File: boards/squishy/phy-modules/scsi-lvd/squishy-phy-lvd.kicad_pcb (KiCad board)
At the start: 6 copper layers, 75 x 92.5 mm, 211 parts, among them J1 SCSI PHY Mezz, J2 SCSI Connector, J3 Conn_01x04, Q1 PMDPB58UPE,115, Q2 PMDPB58UPE,115, Q3 PMDPB58UPE,115, Q4 PMDPB58UPE,115, Q5 PMDPB58UPE,115, Q6 DMN65D8L-7, U1 M24C02-RMC, U10 SN65LVDS180-Q1, U11 SN65LVDS180-Q1, U12 FIN1027A, U13 SN65LVDS180-Q1, U14 SN65LVDS180-Q1, U15 FIN1027A, U16 SN65LVDS180-Q1, U17 SN65LVDS180-Q1, U18 FIN1027A, U19 SN65LVDS180-Q1, U2 SN65LVDS180-Q1, U20 SN65LVDS180-Q1, U21 LM321, U22 SN65LVDS180-Q1, U23 SN65LVDS180-Q1, U24 FIN1027A, U25 SN65LVDS180-Q1, U26 SN65LVDS180-Q1, U27 SN65LVDS180-Q1, U28 SN65LVDS180-Q1, U29 SN65LVDS180-Q1, U3 FIN1027A, U30 SN65LVDS180-Q1, U31 SN65LVDS180-Q1, U34 FIN1027A, U35 FIN1027A, U36 FIN1027A, U37 FIN1027A, U38 UCC5640PW24, U39 LM2903, U4 SN65LVDS180-Q1, U42 SN65LVDS180-Q1, U43 SN65LVDS180-Q1, U44 SN65LVDS180-Q1, U45 SN65LVDS180-Q1, U47 SN65LVDS180-Q1, U5 SN65LVDS180-Q1, U50 UCC5640PW24, U51 UCC5640PW24, U6 FIN1027A, U7 SN65LVDS180-Q1, U8 SN65LVDS180-Q1, U9 FIN1027A

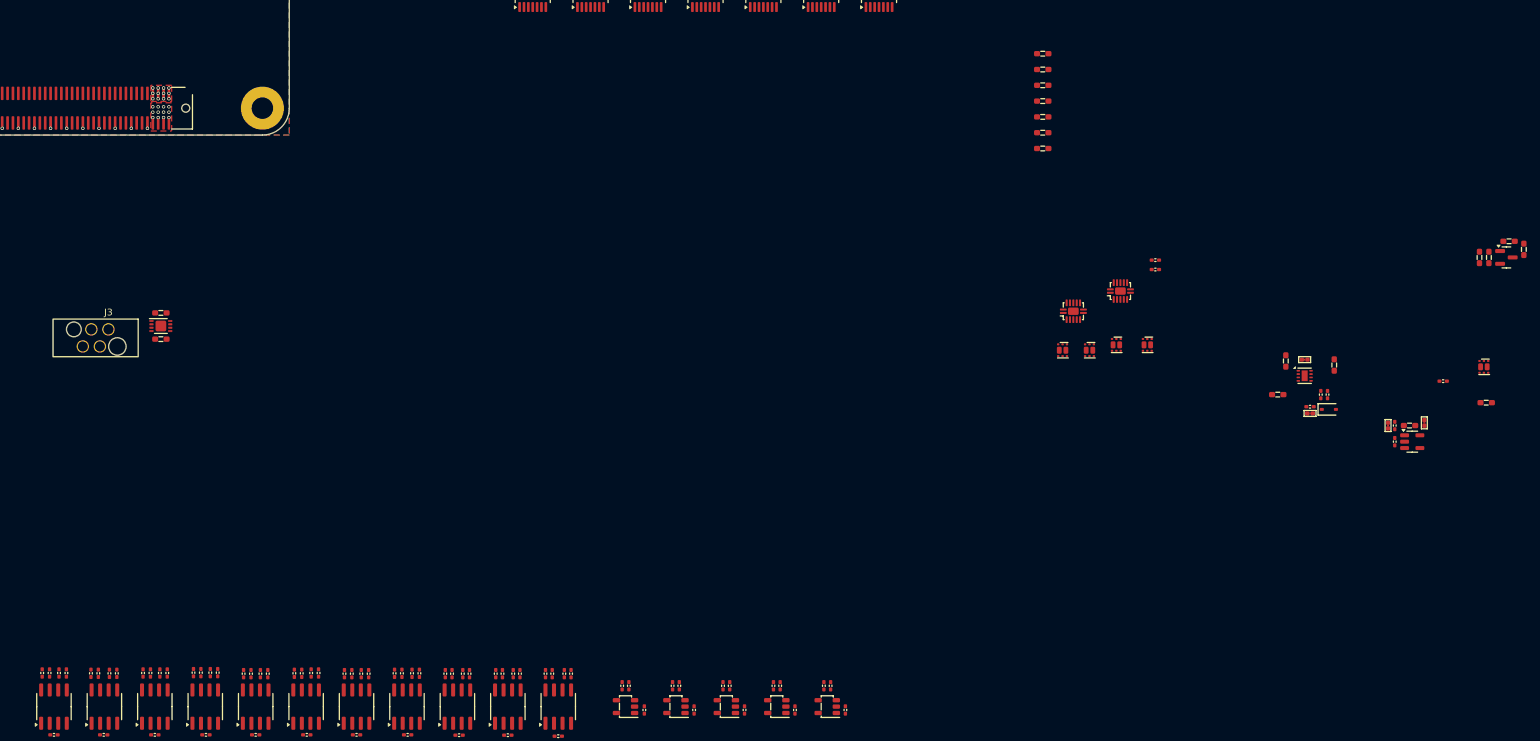
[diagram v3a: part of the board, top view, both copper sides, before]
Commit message: squishy:  phy: lvd: Upgraded to KiCad v9
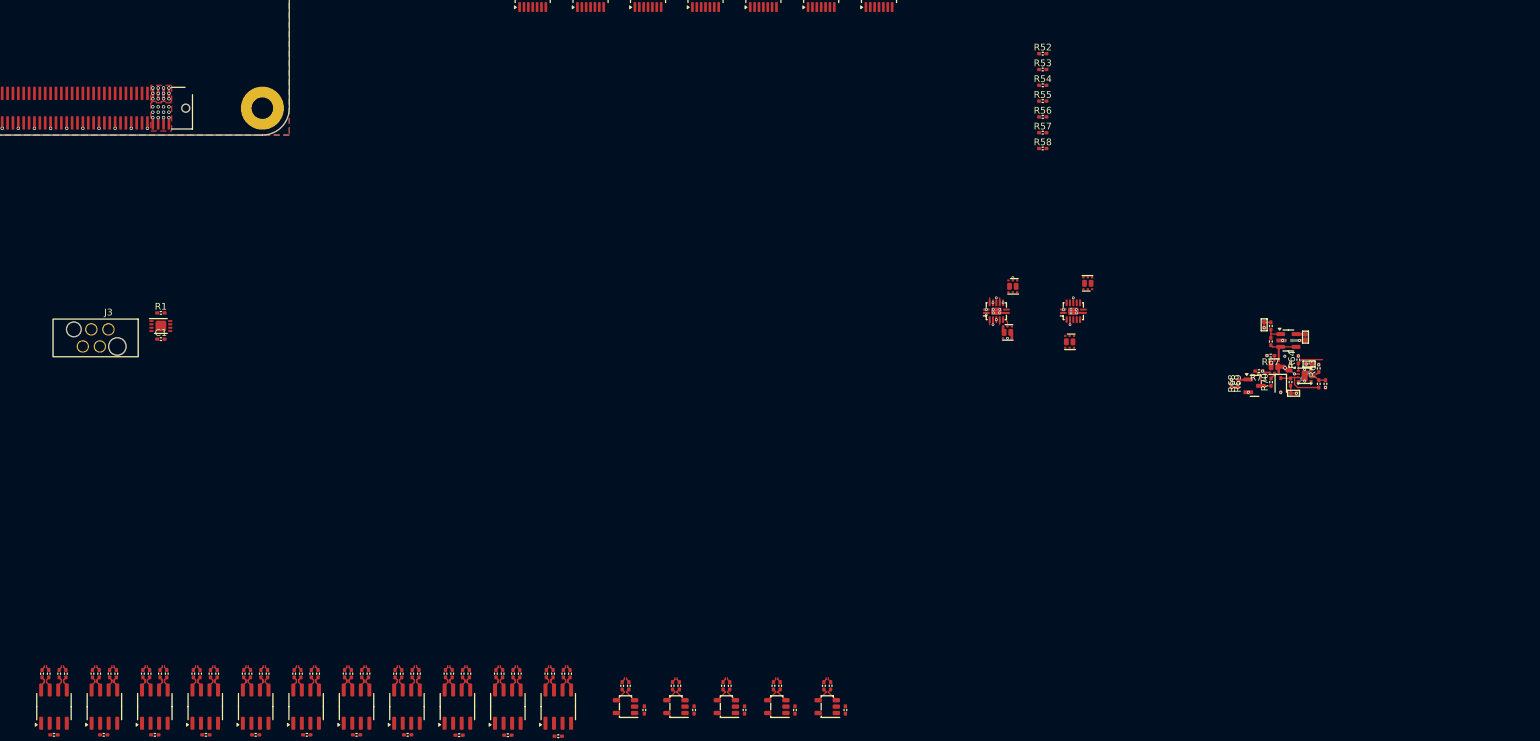
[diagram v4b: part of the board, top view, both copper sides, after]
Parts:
- C1: footprint rhais_rcl:C0603 -> rhais_rcl:C0402
- C64, C65: moved to B.Cu
- C81, C86: footprint rhais_rcl:C0603 -> rhais_rcl:C0402; moved to B.Cu
- R1, R52, R53, R54, R55, R56, R57, R58, R63, R64, R67, R68, R69, R70, R71: footprint rhais_rcl:R0603 -> rhais_rcl:R0402
- moved R70 42.5 mm to (331.0, 176.8)
- moved Q6 42.0 mm to (328.6, 177.3)
- moved R71 41.9 mm to (329.2, 175.1), turned to 180 degrees
- moved R68 41.7 mm to (326.1, 176.9)
- moved R69 41.4 mm to (325.1, 176.9)
- moved R67 32.8 mm to (330.9, 172.8), turned to 180 degrees
- moved Q5 31.2 mm to (331.5, 174.4), turned to 180 degrees
- moved C65 25.3 mm to (289.2, 165.9)
- moved U21 23.8 mm to (333.6, 170.6)
- moved JP3 23.7 mm to (330.0, 168.2)
- moved R65 23.7 mm to (331.0, 170.7)
- moved R66 23.6 mm to (331.0, 168.4)
- moved R61 22.8 mm to (333.9, 174.4), turned to 90 degrees
- moved C86 22.0 mm to (333.6, 170.6)
- moved JP4 21.8 mm to (336.1, 170.1), turned to -90 degrees
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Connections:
- net Net-(C10-Pad1) renamed /Transceivers/DB2E-
- net Net-(C11-Pad1) renamed /Transceivers/DB7E+
- net Net-(C12-Pad1) renamed /Transceivers/DB7E-
- net Net-(C16-Pad1) renamed /Transceivers/DB5E+
- net Net-(C17-Pad1) renamed /Transceivers/DB5E-
- net Net-(C18-Pad1) renamed /Transceivers/DB6E+
- net Net-(C19-Pad1) renamed /Transceivers/DB6E-
- net Net-(C2-Pad1) renamed /Transceivers/DB0E+
- net Net-(C23-Pad1) renamed /Transceivers/DB12E+
- net Net-(C24-Pad1) renamed /Transceivers/DB12E-
- net Net-(C25-Pad1) renamed /Transceivers/DP1E+
- net Net-(C26-Pad1) renamed /Transceivers/DP1E-
- net Net-(C3-Pad1) renamed /Transceivers/DB0E-
- net Net-(C30-Pad1) renamed /Transceivers/DB10E+
- net Net-(C31-Pad1) renamed /Transceivers/DB10E-
- net Net-(C32-Pad1) renamed /Transceivers/DB11E+
- net Net-(C33-Pad1) renamed /Transceivers/DB11E-
- net Net-(C37-Pad1) renamed /Transceivers/DB15E+
- net Net-(C38-Pad1) renamed /Transceivers/DB15E-
- net Net-(C39-Pad1) renamed /Transceivers/DP0E+
- net Net-(C4-Pad1) renamed /Transceivers/DB1E+
- net Net-(C40-Pad1) renamed /Transceivers/DP0E-
- net Net-(C44-Pad1) renamed /Transceivers/ACKE+
- net Net-(C45-Pad1) renamed /Transceivers/ACKE-
- net Net-(C46-Pad1) renamed /Transceivers/RSTE+
- net Net-(C47-Pad1) renamed /Transceivers/RSTE-
- net Net-(C5-Pad1) renamed /Transceivers/DB1E-
- net Net-(C51-Pad1) renamed /Transceivers/DB3E+
- net Net-(C52-Pad1) renamed /Transceivers/DB3E-
- net Net-(C53-Pad1) renamed /Transceivers/DB4E+
- net Net-(C54-Pad1) renamed /Transceivers/DB4E-
- net Net-(C58-Pad1) renamed /Transceivers/DB8E+
- net Net-(C59-Pad1) renamed /Transceivers/DB13E+
- net Net-(C60-Pad1) renamed /Transceivers/ATNE+
- net Net-(C61-Pad1) renamed /Transceivers/SELE+
- net Net-(C62-Pad1) renamed /Transceivers/MSGE+
- net Net-(C63-Pad1) renamed /Transceivers/REQE+
- net Net-(C66-Pad1) renamed /Transceivers/DB8E-
- net Net-(C67-Pad1) renamed /Transceivers/DB13E-
- net Net-(C68-Pad1) renamed /Transceivers/ATNE-
- net Net-(C69-Pad1) renamed /Transceivers/SELE-
- net Net-(C70-Pad1) renamed /Transceivers/MSGE-
- net Net-(C71-Pad1) renamed /Transceivers/REQE-
- net Net-(C74-Pad1) renamed /Transceivers/DB9E+
- net Net-(C75-Pad1) renamed /Transceivers/DB14E+
- net Net-(C76-Pad1) renamed /Transceivers/BSYE+
- net Net-(C77-Pad1) renamed /Transceivers/C/DE+
- net Net-(C79-Pad1) renamed /Transceivers/I/OE+
- net Net-(C82-Pad1) renamed /Transceivers/DB9E-
- net Net-(C83-Pad1) renamed /Transceivers/DB14E-
- net Net-(C84-Pad1) renamed /Transceivers/BSYE-
- net Net-(C85-Pad1) renamed /Transceivers/C/DE-
- net Net-(C87-Pad1) renamed /Transceivers/I/OE-
- net Net-(C9-Pad1) renamed /Transceivers/DB2E+
- U39 pad 9: (no net) -> GND
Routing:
- net /CON.DIFFSENSE: track 0.00 -> 7.83 mm, vias 0 -> 3
- net Net-(D1-K): track 0.00 -> 7.51 mm
- net Net-(Q5A-S): track 0.00 -> 6.04 mm
- net /PHY.LS_CTRL0: track 0.00 -> 5.86 mm, vias 0 -> 4
- net GND: track 0.00 -> 5.38 mm, vias 34 -> 50
- net /~{HVD}: track 0.00 -> 4.93 mm
- net /Transceivers/DBL_EMPH_EN: track 0.00 -> 4.66 mm, vias 0 -> 2
- net Net-(Q6-D): track 0.00 -> 4.06 mm
- net +5V: track 0.00 -> 2.92 mm, vias 12 -> 16
- net Net-(U21-+): track 0.00 -> 2.66 mm
- net Net-(U39B--): track 0.00 -> 2.32 mm
- net /Transceivers/SELE-: track 0.00 -> 2.23 mm
- net /Transceivers/SELE+: track 0.00 -> 2.23 mm
- net /Transceivers/BSYE-: track 0.00 -> 2.23 mm
- net /Transceivers/BSYE+: track 0.00 -> 2.23 mm
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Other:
- board text added: "0.2028mm"
- board text added: "0.2104mm"
- board text added: "0.4000mm"
- board text added: "IFF JLCPCB: JLC06161H-7628"
- board text added: "Impedance Table: 50Ω Coplanar Single Ended (inner): width: 0.2949mm space: 0.2 72Ω Coplanar Single Ended (outter): width: 0.1115mm 72Ω Non-Coplanar Single Ended (outter): width: 0.1514mm 50Ω Non-Coplanar Single Ended (inner): width: 0.3493mm 120Ω Coplanar Differential (outter): width: 0.1148, space: 0.2mm 120Ω Non-Coplanar Differential (outter): width: 0.1275, space: 0.2mm"
- board text added: "Outter Copper: 1oz Inner Copper: 0.5oz"
- board text added: "Prepreg (7628*1)"
- board text removed: "0.0994mm"
- board text removed: "0.1088mm"
- board text removed: "0.5500mm"
- board text removed: "IFF JLCPCB: JLC06161H-3313"
- board text removed: "Impedance Table: 50Ω Coplanar Signle Ended (inner): width: TODO 50Ω Coplanar Signle Ended (outter): width: TODO 50Ω Non-Coplanar Signle Ended (inner): width: TODO 50Ω Non-Coplanar Signle Ended (outter): width: TODO"
- board text removed: "Outter Copper: 1Oz Inner Copper: 0.5Oz"
- board text removed: "Prepreg (2116*1)"
- board text removed: "Prepreg (3313*1)"
